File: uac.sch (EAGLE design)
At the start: 183 parts, among them Y1 RESONATORSMD

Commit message: Placing components, change to custom components
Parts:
- C20: device SparkFun:CAP0603 -> Custom components:C-EUC0603
- C8: device devergy_berkelaarmrt:C0603_1UF -> Custom components:C-EUC0603
- R13, R15, R16, R23, R31, R36, R43: device rcl:R-EU_R0603 -> Custom components:R-EU_R0603
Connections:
- net N$5: now also U$2.P$1; no longer U$2.P$4
- net N$6: now also U$2.P$4; no longer U$2.P$1
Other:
- moved on the sheet: C1, C10, C11, C12, C13, C14, C15, C2, C20, C3, C4, C5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

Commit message: Start power subsystem
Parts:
- added BAT: (no value), Custom components:M02-JST-2MM-SMT
- added C16, C17, C23: 10u, Custom components:C-EUC0603
- added C18: 100n, Custom components:C-EUC0603
- added C19: 10p, Custom components:C-EUC0603
- added C21: 56n, Custom components:C-EUC0603
- added C22: 4.7u, Custom components:C-EUC0603
- added IC1: (no value), Custom components:V_REG_LM1117SOT223
- added L3: 1.5uH, Custom components:INDUCTOR_VLF4012
- added PC1, PC2: 47u, rcl:CPOL-EUD
- added R18: 187k, Custom components:R-EU_R0603
- added R19: 60.4k, Custom components:R-EU_R0603
- added R20: 15k, Custom components:R-EU_R0603
- added R21: 3k, Custom components:R-EU_R0603
- added R22: 10k/NTC, Custom components:R-EU_R0603
- added U$10: DIODE_VS10BQ015PBF, Custom components:DIODE_VS10BQ015PBF
- added U$3: 5V, Custom components:SC4503
- added U1: MCP73833-FCI/UN, Custom components:MCP73833-FCI/UN
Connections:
- new net +5V: C18.1, C19.1, C23.1, IC1.IN, PC2.+, R18.1, U$10.C
- new net N$19: C19.2, R18.2, R19.1, U$3.FB
- new net N$20: L3.P$2, U$10.A, U$3.SW
- new net N$21: R21.2, U1.PROG
- new net N$22: C21.1, R20.2, U$3.SS
- new net N$27: R22.2, U1.THERM
- new net STAT1: U$1PORT_E.P12, U1.STAT1
- new net STAT2: U$1PORT_E.P13, U1.STAT2
- new net VBAT: BAT.1, C16.1, C22.1, L3.P$1, R20.1, U$3.VIN, U1.VBAT, U1.VBAT_2
- new net V_CHARGE: U1.VDD, U1.VDD_2
- net +3V3: now also C17.1, IC1.OUT, IC1.OUT@1, PC1.+
- net GND: now also BAT.2, C16.2, C17.2, C18.2, C21.2, C22.2, C23.2, IC1.ADJ, PC1.-, PC2.-, R19.2, R21.1, R22.1, U$3.GND, U1.VSS
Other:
- note added: "Boost"
- note added: "C21, 4.7uF, digikey: 490-3297-1-ND"
- note added: "Charging"
- note added: "Extra capacitoren, stabilisatie"
- note added: "Misschien vervangen door sepic converter (datasheet)"
- moved on the sheet: C1, C10, C11, C12, C13, C14, C15, C2, C20, C3, C4, C5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

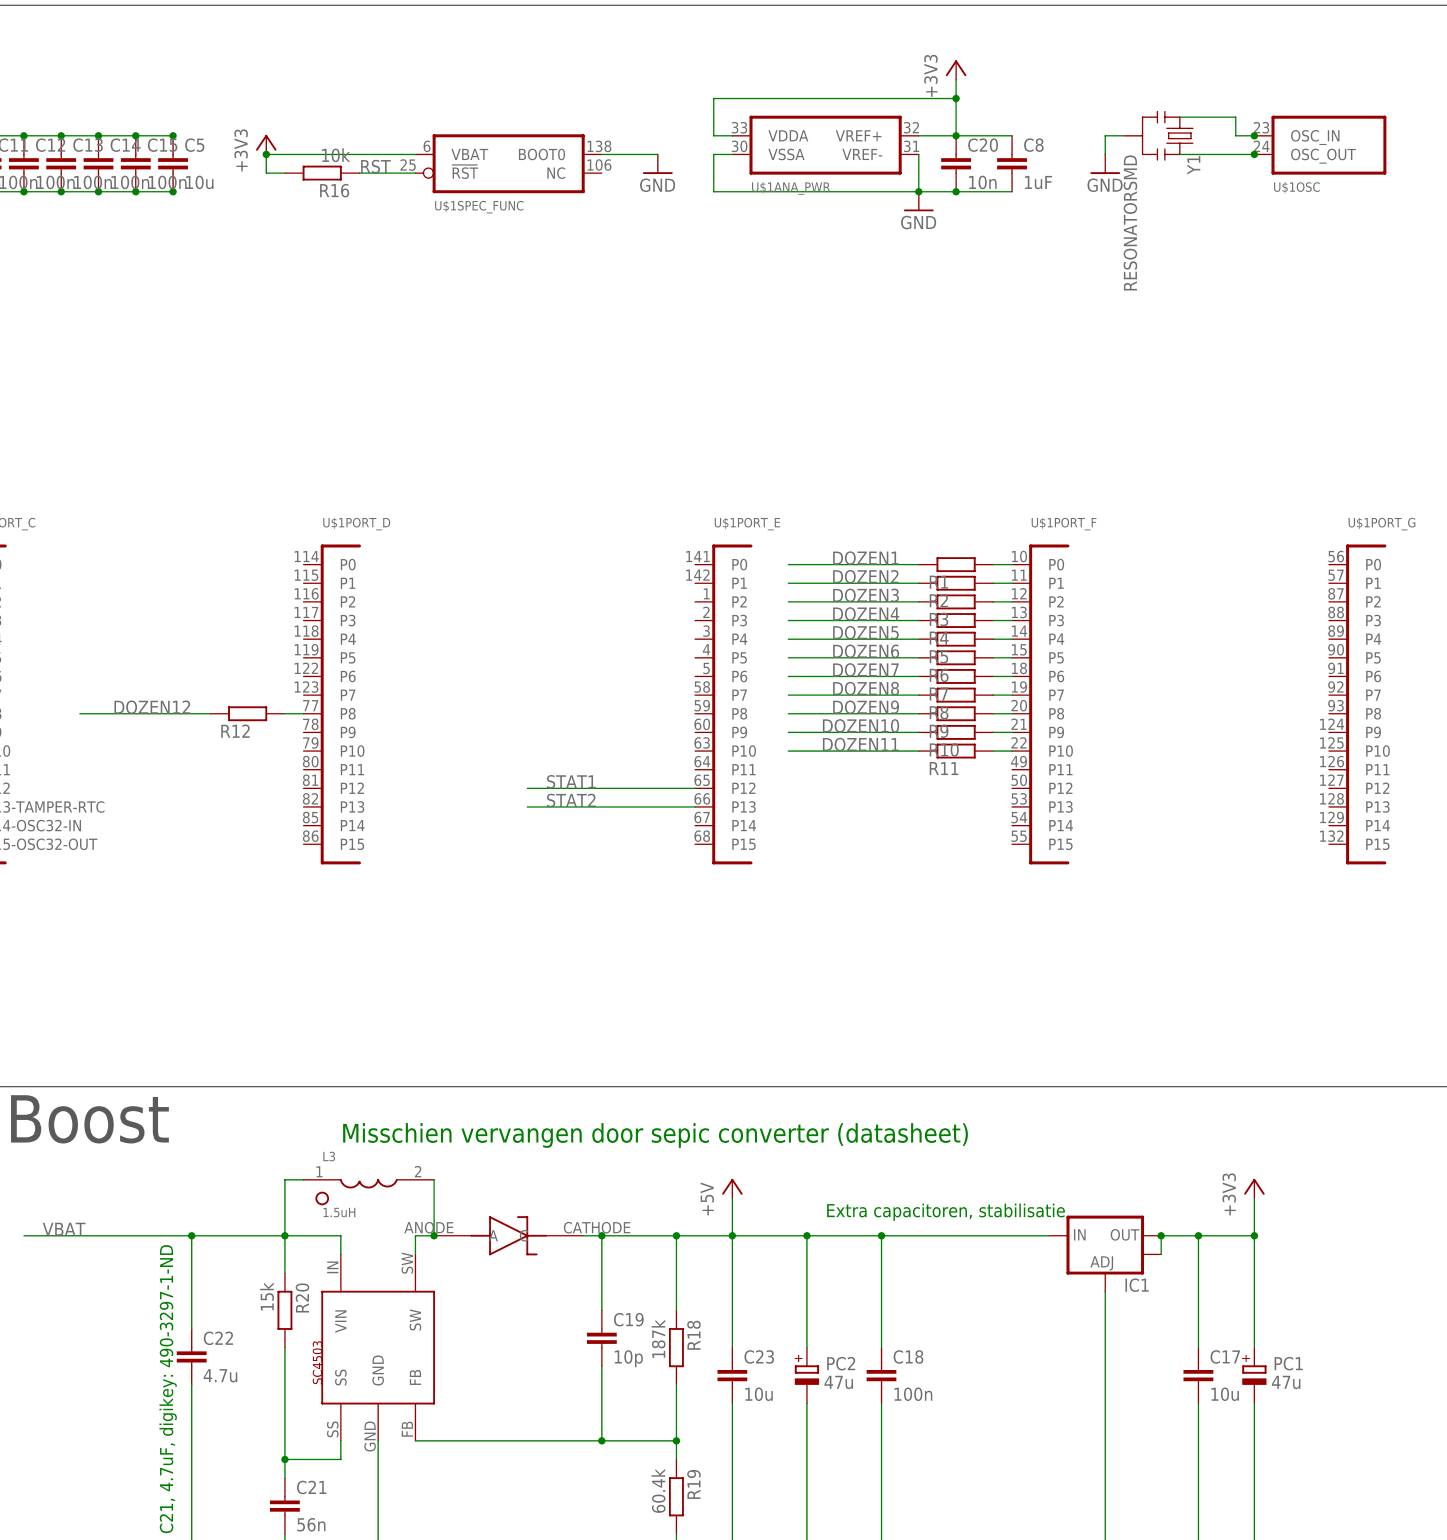
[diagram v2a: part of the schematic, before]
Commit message: Layout power system
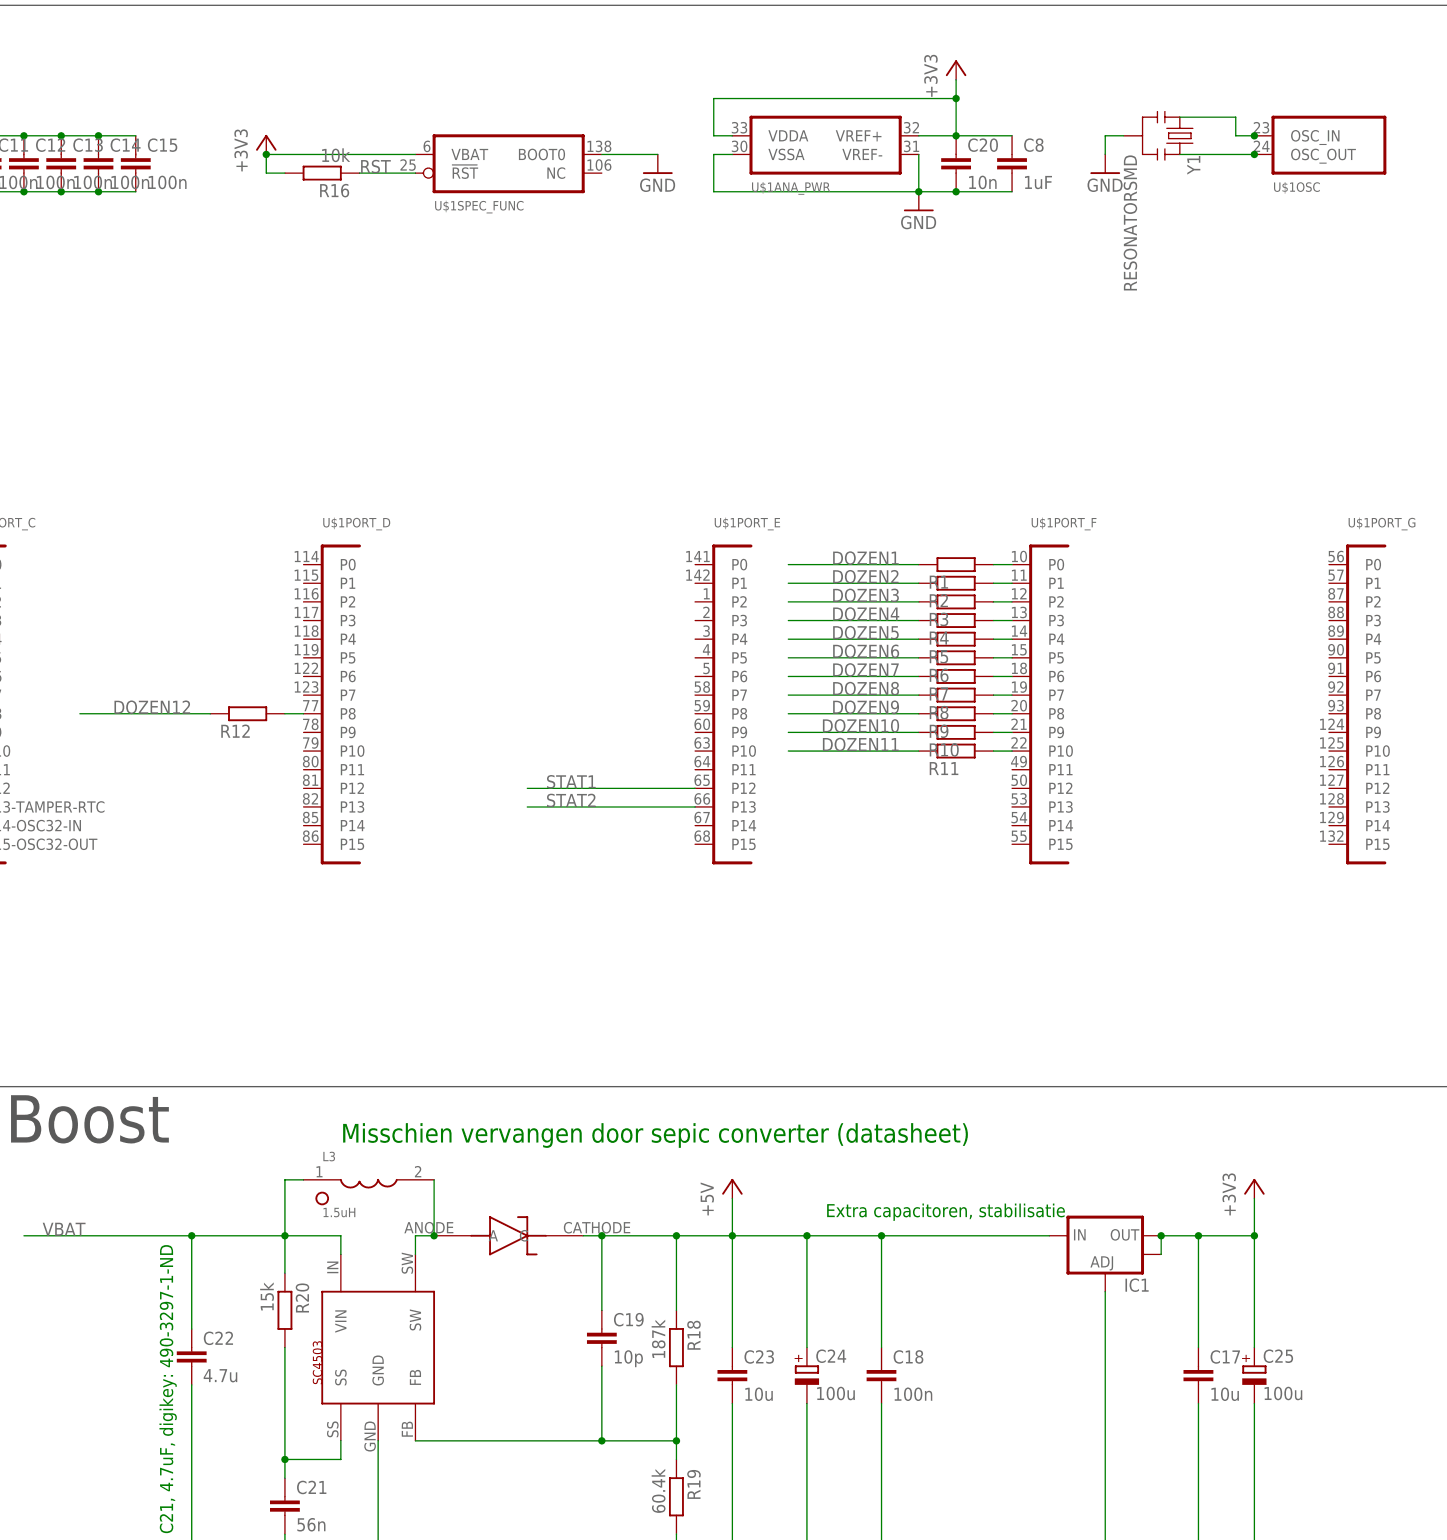
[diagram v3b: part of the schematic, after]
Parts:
- removed C5: 10u, Custom components:C-EUC0603
- removed PC1, PC2: 47u, rcl:CPOL-EUD
- added C24, C25: 100u, Custom components:CPOL-EUSMCC
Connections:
- net +3V3: now also C25.+; no longer C5.1, PC1.+
- net +5V: now also C24.+; no longer PC2.+
- net GND: now also C24.-, C25.-; no longer C5.2, PC1.-, PC2.-
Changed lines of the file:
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@@
 <part name="Y1" library="Custom components" deviceset="RESONATOR" device="SMD"/>
 <part name="GND2" library="Custom components" deviceset="GND" device=""/>
-<part name="C5" library="Custom components" deviceset="C-EU" device="C0603" value="10u"/>
 <part name="MASTER_PROG" library="Custom components" deviceset="PINHD-2X3" device="SMT"/>
 <part name="GND19" library="supply1" deviceset="GND" device=""/>
@@
 <part name="GND41" library="supply1" deviceset="GND" device=""/>
 <part name="GND42" library="supply1" deviceset="GND" device=""/>
-<part name="PC2" library="rcl" deviceset="CPOL-EU" device="D" value="47u"/>
 <part name="GND4" library="supply1" deviceset="GND" device=""/>
 <part name="C18" library="Custom components" deviceset="C-EU" device="C0603" value="100n"/>
@@
 <part name="+3V1" library="Custom components" deviceset="+3V3" device=""/>
 <part name="C17" library="Custom components" deviceset="C-EU" device="C0603" value="10u"/>
-<part name="PC1" library="rcl" deviceset="CPOL-EU" device="D" value="47u"/>
 <part name="BAT" library="Custom components" deviceset="M02" device="-JST-2MM-SMT"/>
 <part name="GND5" library="supply1" deviceset="GND" device=""/>
+<part name="C24" library="Custom components" deviceset="CPOL-EU" device="SMCC" value="100u"/>
+<part name="C25" library="Custom components" deviceset="CPOL-EU" device="SMCC" value="100u"/>
 </parts>
 <sheets>
@@
 <instance part="Y1" gate="G$1" x="701.04" y="248.92" rot="R270"/>
 <instance part="GND2" gate="1" x="690.88" y="243.84"/>
-<instance part="C5" gate="G$1" x="563.88" y="246.38"/>
 <instance part="MASTER_PROG" gate="A" x="411.48" y="233.68"/>
 <instance part="GND19" gate="1" x="388.62" y="238.76"/>
@@
 <instance part="GND41" gate="1" x="424.18" y="63.5"/>
 <instance part="GND42" gate="1" x="474.98" y="58.42"/>
-<instance part="PC2" gate="G$1" x="650.24" y="81.28" smashed="yes">
-<attribute name="NAME" x="652.78" y="80.7466" size="1.778" layer="95"/>
-<attribute name="VALUE" x="652.526" y="78.2066" size="1.778" layer="96"/>
-</instance>
 <instance part="GND4" gate="1" x="650.24" y="38.1"/>
 <instance part="C18" gate="G$1" x="660.4" y="81.28"/>
@@
 <instance part="+3V1" gate="G$1" x="711.2" y="106.68"/>
 <instance part="C17" gate="G$1" x="703.58" y="81.28"/>
-<instance part="PC1" gate="G$1" x="711.2" y="81.28" smashed="yes">
-<attribute name="NAME" x="713.74" y="80.7466" size="1.778" layer="95"/>
-<attribute name="VALUE" x="713.486" y="78.2066" size="1.778" layer="96"/>
-</instance>
 <instance part="BAT" gate="G$1" x="398.78" y="35.56" rot="MR180"/>
 <instance part="GND5" gate="1" x="408.94" y="27.94"/>
+<instance part="C24" gate="G$1" x="650.24" y="81.28"/>
+<instance part="C25" gate="G$1" x="711.2" y="81.28"/>
 </instances>
 <busses>
@@
 <junction x="508" y="241.3"/>
 <pinref part="C15" gate="G$1" pin="2"/>
-<wire x1="563.88" y1="241.3" x2="558.8" y2="241.3" width="0.1524" layer="91"/>
 <pinref part="C14" gate="G$1" pin="2"/>
 <wire x1="558.8" y1="241.3" x2="553.72" y2="241.3" width="0.1524" layer="91"/>
@@
 <wire x1="533.4" y1="241.3" x2="528.32" y2="241.3" width="0.1524" layer="91"/>
 <wire x1="528.32" y1="241.3" x2="523.24" y2="241.3" width="0.1524" layer="91"/>
-<junction x="558.8" y="241.3"/>
 <junction x="553.72" y="241.3"/>
 <junction x="548.64" y="241.3"/>
@@
 <junction x="533.4" y="241.3"/>
 <junction x="528.32" y="241.3"/>
-<pinref part="C5" gate="G$1" pin="2"/>
-<junction x="563.88" y="241.3"/>
 </segment>
 <segment>
@@
 <wire x1="566.42" y1="55.88" x2="579.12" y2="55.88" width="0.1524" layer="91"/>
 <junction x="579.12" y="55.88"/>
-<pinref part="PC2" gate="G$1" pin="-"/>
 <pinref part="GND4" gate="1" pin="GND"/>
 <wire x1="650.24" y1="40.64" x2="650.24" y2="55.88" width="0.1524" layer="91"/>
@@
 <wire x1="690.88" y1="55.88" x2="703.58" y2="55.88" width="0.1524" layer="91"/>
 <wire x1="703.58" y1="55.88" x2="703.58" y2="76.2" width="0.1524" layer="91"/>
-<pinref part="PC1" gate="G$1" pin="-"/>
 <wire x1="703.58" y1="55.88" x2="711.2" y2="55.88" width="0.1524" layer="91"/>
 <wire x1="711.2" y1="55.88" x2="711.2" y2="76.2" width="0.1524" layer="91"/>
 <junction x="703.58" y="55.88"/>
 <junction x="690.88" y="55.88"/>
+<pinref part="C24" gate="G$1" pin="-"/>
+<pinref part="C25" gate="G$1" pin="-"/>
 </segment>
 <segment>
@@
 <pinref part="C15" gate="G$1" pin="1"/>
 <wire x1="553.72" y1="248.92" x2="558.8" y2="248.92" width="0.1524" layer="91"/>
-<wire x1="558.8" y1="248.92" x2="563.88" y2="248.92" width="0.1524" layer="91"/>
 <junction x="523.24" y="248.92"/>
 <junction x="528.32" y="248.92"/>
@@
 <junction x="548.64" y="248.92"/>
 <junction x="553.72" y="248.92"/>
-<junction x="558.8" y="248.92"/>
-<pinref part="C5" gate="G$1" pin="1"/>
-<junction x="563.88" y="248.92"/>
 </segment>
 <segment>
@@
 <pinref part="C17" gate="G$1" pin="1"/>
 <wire x1="703.58" y1="83.82" x2="703.58" y2="99.06" width="0.1524" layer="91"/>
-<pinref part="PC1" gate="G$1" pin="+"/>
 <wire x1="711.2" y1="83.82" x2="711.2" y2="99.06" width="0.1524" layer="91"/>
 <junction x="703.58" y="99.06"/>
 <junction x="711.2" y="99.06"/>
+<pinref part="C25" gate="G$1" pin="+"/>
 </segment>
 </net>
@@
 <wire x1="640.08" y1="104.14" x2="640.08" y2="99.06" width="0.1524" layer="91"/>
 <wire x1="650.24" y1="83.82" x2="650.24" y2="99.06" width="0.1524" layer="91"/>
-<pinref part="PC2" gate="G$1" pin="+"/>
 <pinref part="C18" gate="G$1" pin="1"/>
 <wire x1="650.24" y1="99.06" x2="660.4" y2="99.06" width="0.1524" layer="91"/>
@@
 <wire x1="683.26" y1="99.06" x2="660.4" y2="99.06" width="0.1524" layer="91"/>
 <junction x="660.4" y="99.06"/>
-</segment>
-</net>
+<pinref part="C24" gate="G$1" pin="+"/>
+</segment>
+</net>

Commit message: Modified schematic, added adxl345
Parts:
- added C26, C5: 100n, Custom components:C-EUC0603
- added C27: 10u, Custom components:C-EUC0603
- added U2: ADXL345, SparkFun2012:ADXL345
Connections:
- net +3V3: now also C26.1, C27.1, C5.1, U2.VDD, U2.VSS
- net GND: now also C26.2, C27.2, C5.2, U2.GND@2, U2.GND@4, U2.GND@5
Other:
- note added: "AcceleroMeter"
- note added: "MicroController"
- note added: "Sound"
- note added: "WakeUp Light"
- moved on the sheet: BAT, C1, C10, C11, C12, C13, C14, C15, C16, C17, C18, C19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

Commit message: Connected the accelerometer adxl345
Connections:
- new net ADXL345_INT1: U$1PORT_D.P0, U2.INT1
- new net ADXL345_INT2: U$1PORT_D.P1, U2.INT2
- new net SPI1_MISO: U$1PORT_A.P6, U2.SDO
- new net SPI1_MOSI: U$1PORT_A.P7, U2.SDA
- new net SPI1_NSS: U$1PORT_A.P4, U2.CS
- new net SPI1_SCK: U$1PORT_A.P5, U2.SCL
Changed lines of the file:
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@@
+</segment>
+</net>
+<net name="SPI1_NSS" class="0">
+<segment>
+<pinref part="U$1" gate="PORT_A" pin="P4"/>
+<wire x1="45.72" y1="182.88" x2="20.32" y2="182.88" width="0.1524" layer="91"/>
+<label x="22.86" y="182.88" size="1.778" layer="95"/>
+</segment>
+<segment>
+<pinref part="U2" gate="G$1" pin="CS"/>
+<wire x1="434.34" y1="66.04" x2="454.66" y2="66.04" width="0.1524" layer="91"/>
+<label x="436.88" y="66.04" size="1.778" layer="95"/>
+</segment>
+</net>
+<net name="SPI1_SCK" class="0">
+<segment>
+<pinref part="U$1" gate="PORT_A" pin="P5"/>
+<wire x1="45.72" y1="180.34" x2="20.32" y2="180.34" width="0.1524" layer="91"/>
+<label x="22.86" y="180.34" size="1.778" layer="95"/>
+</segment>
+<segment>
+<pinref part="U2" gate="G$1" pin="SCL"/>
+<wire x1="434.34" y1="55.88" x2="454.66" y2="55.88" width="0.1524" layer="91"/>
+<label x="436.88" y="55.88" size="1.778" layer="95"/>
+</segment>
+</net>
+<net name="SPI1_MISO" class="0">
+<segment>
+<pinref part="U$1" gate="PORT_A" pin="P6"/>
+<wire x1="45.72" y1="177.8" x2="20.32" y2="177.8" width="0.1524" layer="91"/>
+<label x="22.86" y="177.8" size="1.778" layer="95"/>
+</segment>
+<segment>
+<pinref part="U2" gate="G$1" pin="SDO"/>
+<wire x1="434.34" y1="60.96" x2="454.66" y2="60.96" width="0.1524" layer="91"/>
+<label x="436.88" y="60.96" size="1.778" layer="95"/>
+</segment>
+</net>
+<net name="SPI1_MOSI" class="0">
+<segment>
+<pinref part="U$1" gate="PORT_A" pin="P7"/>
+<wire x1="45.72" y1="175.26" x2="20.32" y2="175.26" width="0.1524" layer="91"/>
+<label x="22.86" y="175.26" size="1.778" layer="95"/>
+</segment>
+<segment>
+<pinref part="U2" gate="G$1" pin="SDA"/>
+<wire x1="434.34" y1="58.42" x2="454.66" y2="58.42" width="0.1524" layer="91"/>
+<label x="436.88" y="58.42" size="1.778" layer="95"/>
+</segment>
+</net>
+<net name="ADXL345_INT1" class="0">
+<segment>
+<pinref part="U$1" gate="PORT_D" pin="P0"/>
+<wire x1="205.74" y1="190.5" x2="177.8" y2="190.5" width="0.1524" layer="91"/>
+<label x="180.34" y="190.5" size="1.778" layer="95"/>
+</segment>
+<segment>
+<pinref part="U2" gate="G$1" pin="INT1"/>
+<wire x1="434.34" y1="50.8" x2="454.66" y2="50.8" width="0.1524" layer="91"/>
+<label x="436.88" y="50.8" size="1.778" layer="95"/>
+</segment>
+</net>
+<net name="ADXL345_INT2" class="0">
+<segment>
+<pinref part="U$1" gate="PORT_D" pin="P1"/>
+<wire x1="205.74" y1="187.96" x2="177.8" y2="187.96" width="0.1524" layer="91"/>
+<label x="180.34" y="187.96" size="1.778" layer="95"/>
+</segment>
+<segment>
+<pinref part="U2" gate="G$1" pin="INT2"/>
+<wire x1="434.34" y1="48.26" x2="454.66" y2="48.26" width="0.1524" layer="91"/>
+<label x="436.88" y="48.26" size="1.778" layer="95"/>
 </segment>
 </net>

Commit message: Wake Up Leds 5mm
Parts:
- added Q1, Q2, Q3, Q4, Q5: 2N7002CK4SST, Custom components:2N7002CK4SST
- added R14, R17, R24, R25, R26: 200, Custom components:R-EU_R0603
- added U$4, U$5, U$6, U$7, U$8: LED_5MM_SMD, timearc:LED_5MM_SMD
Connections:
- new net N$23: Q1.D, U$4.P$2
- new net N$24: Q2.D, U$5.P$2
- new net N$25: Q3.D, U$6.P$2
- new net N$26: Q4.D, U$7.P$2
- new net N$28: Q5.D, U$8.P$2
- new net N$29: R14.1, U$4.P$1
- new net N$30: R17.1, U$5.P$1
- new net N$31: R24.1, U$6.P$1
- new net N$32: R25.1, U$7.P$1
- new net N$33: R26.1, U$8.P$1
- new net WAKE1: Q1.G
- new net WAKE2: Q2.G
- new net WAKE3: Q3.G
- new net WAKE4: Q4.G
- new net WAKE5: Q5.G
- net +5V: now also R14.2, R17.2, R24.2, R25.2, R26.2
- net ADXL345_INT1: now also U$1PORT_B.P0; no longer U$1PORT_D.P0
- net ADXL345_INT2: now also U$1PORT_B.P1; no longer U$1PORT_D.P1
- net GND: now also Q1.S, Q2.S, Q3.S, Q4.S, Q5.S
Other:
- note added: "Light sensor"
- note added: "Serial"
- note added: "Wifi"
- note removed: "Extra capacitoren, stabilisatie"
- moved on the sheet: C17, C25, HOUR0, HOUR1, HOUR10, HOUR11, HOUR2, HOUR3, HOUR4, HOUR5, HOUR6, HOUR7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
